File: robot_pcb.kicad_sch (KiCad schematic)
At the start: 47 parts, among them J1 Raspberry_Pi_2_3, J10 Servo_TrayRelease, J11 BATT BYPASS, J12 12V BYPASS, J13 MAX14870, J14 MAX14870, J15 MAX14870, J16 MAX14870, J17 Conn_01x04, J18 USB_C_Receptacle_PowerOnly_6P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

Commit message: parts
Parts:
- C10, C11, C12, C13, C14, C15, C16, C6, C69, C7, C70, C8, C9: footprint (none) -> Capacitor_SMD:C_0402_1005Metric
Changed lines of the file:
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@@
 			)
 		)
-		(property "Footprint" ""
+		(property "Footprint" "Capacitor_SMD:C_0402_1005Metric"
 			(at 220.6752 102.87 0)
 			(effects
@@
 			)
 		)
-		(property "Footprint" ""
+		(property "Footprint" "Capacitor_SMD:C_0402_1005Metric"
 			(at 194.0052 48.26 0)
 			(effects
@@
 			)
 		)
-		(property "Footprint" ""
+		(property "Footprint" "Capacitor_SMD:C_0402_1005Metric"
 			(at 206.7052 48.26 0)
 			(effects
@@
 			)
 		)
-		(property "Footprint" ""
+		(property "Footprint" "Capacitor_SMD:C_0402_1005Metric"
 			(at 324.8152 48.26 0)
 			(effects
@@
 			)
 		)
-		(property "Footprint" ""
+		(property "Footprint" "Capacitor_SMD:C_0402_1005Metric"
 			(at 244.8052 48.26 0)
 			(effects
@@
 			)
 		)
-		(property "Footprint" ""
+		(property "Footprint" "Capacitor_SMD:C_0402_1005Metric"
 			(at 309.5752 48.26 0)
 			(effects
@@
 			)
 		)
-		(property "Footprint" ""
+		(property "Footprint" "Capacitor_SMD:C_0402_1005Metric"
 			(at 352.7552 48.26 0)
 			(effects
@@
 			)
 		)
-		(property "Footprint" ""
+		(property "Footprint" "Capacitor_SMD:C_0402_1005Metric"
 			(at 238.4552 102.87 0)
 			(effects
@@
 			)
 		)
-		(property "Footprint" ""
+		(property "Footprint" "Capacitor_SMD:C_0402_1005Metric"
 			(at 270.2052 48.26 0)
 			(effects
@@
 			)
 		)
-		(property "Footprint" ""
+		(property "Footprint" "Capacitor_SMD:C_0402_1005Metric"
 			(at 232.1052 48.26 0)
 			(effects
@@
 			)
 		)
-		(property "Footprint" ""
+		(property "Footprint" "Capacitor_SMD:C_0402_1005Metric"
 			(at 211.1248 62.23 0)
 			(effects
@@
 			)
 		)
-		(property "Footprint" ""
+		(property "Footprint" "Capacitor_SMD:C_0402_1005Metric"
 			(at 219.4052 48.26 0)
 			(effects
@@
 			)
 		)
-		(property "Footprint" ""
+		(property "Footprint" "Capacitor_SMD:C_0402_1005Metric"
 			(at 257.5052 48.26 0)
 			(effects

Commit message: part numebrs
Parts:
- C10, C11, C16, C6, C7, C8, C9: LCSC (none) -> C307331
- C12: footprint Capacitor_SMD:C_0402_1005Metric -> Capacitor_SMD:C_0603_1608Metric; LCSC (none) -> C96446
- C13: LCSC (none) -> C15195
- C14, C15: LCSC (none) -> C52923
- C69, C70: LCSC (none) -> C86285

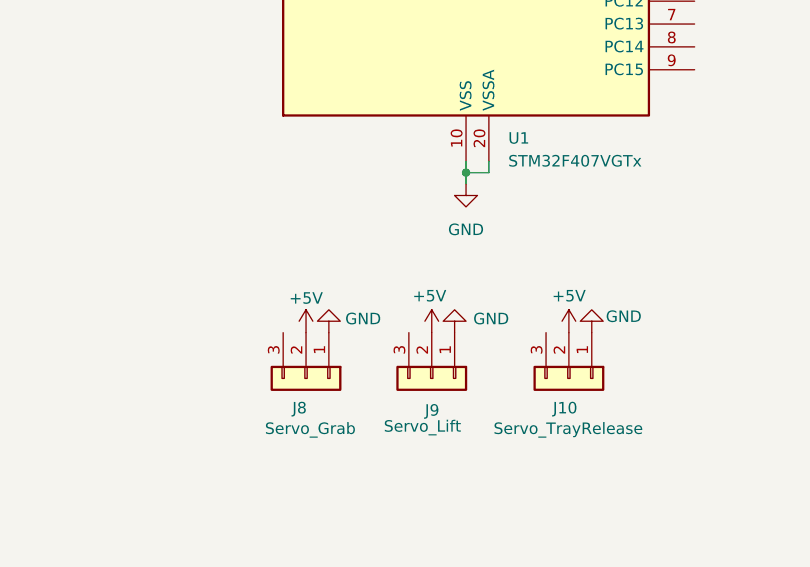
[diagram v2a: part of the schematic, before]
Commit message: added pwm to servos
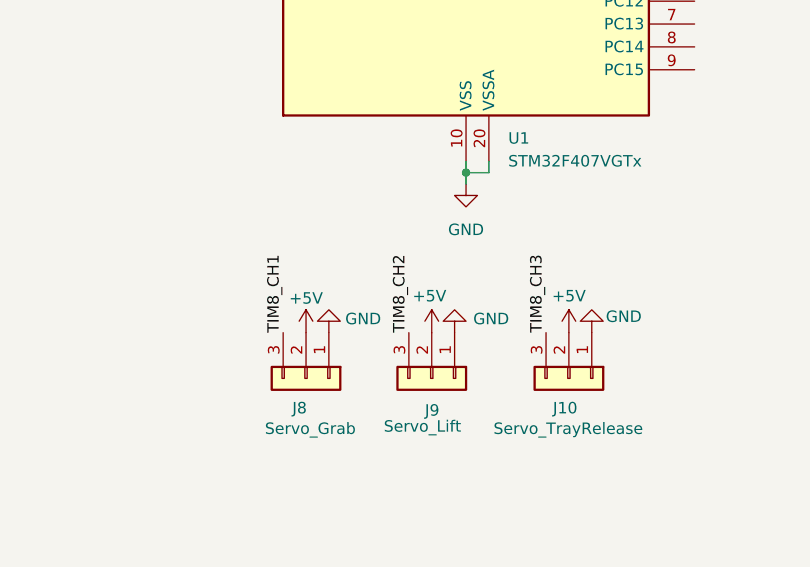
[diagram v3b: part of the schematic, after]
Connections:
- net TIM8_CH1: now also J8.3 (Pin_3)
- net TIM8_CH2: now also J9.3 (Pin_3)
- net TIM8_CH3: now also J10.3 (Pin_3)
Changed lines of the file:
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@@
+		)
+	)
+	(label "TIM8_CH2"
+		(at 284.48 214.63 90)
+		(effects
+			(font
+				(size 1.27 1.27)
+			)
+			(justify left bottom)
 		)
 	)
@@
 		)
 	)
+	(label "TIM8_CH1"
+		(at 270.51 214.63 90)
+		(effects
+			(font
+				(size 1.27 1.27)
+			)
+			(justify left bottom)
+		)
+	)
 	(label "BR_M2"
 		(at 124.46 261.62 0)
@@
 		(effects
 			(font
+				(size 1.27 1.27)
+			)
+			(justify left bottom)
+		)
+	)
+	(label "TIM8_CH3"
+		(at 299.72 214.63 90)
+		(effects
+			(font

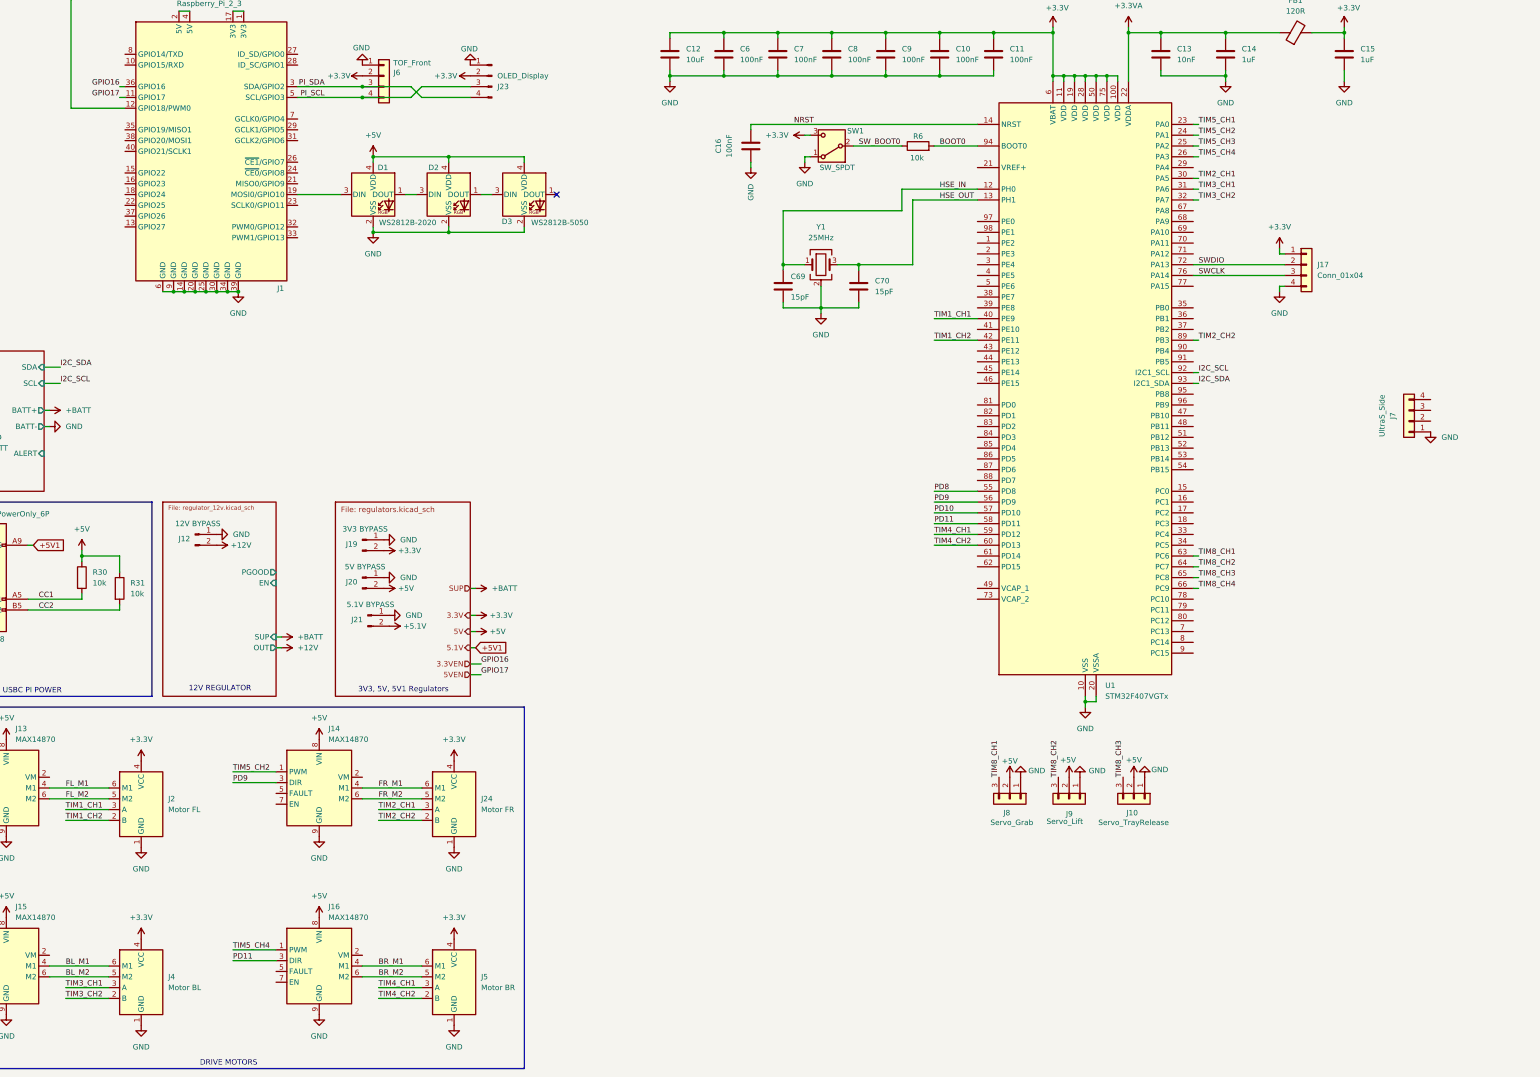
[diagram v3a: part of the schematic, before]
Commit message: Added BNO086
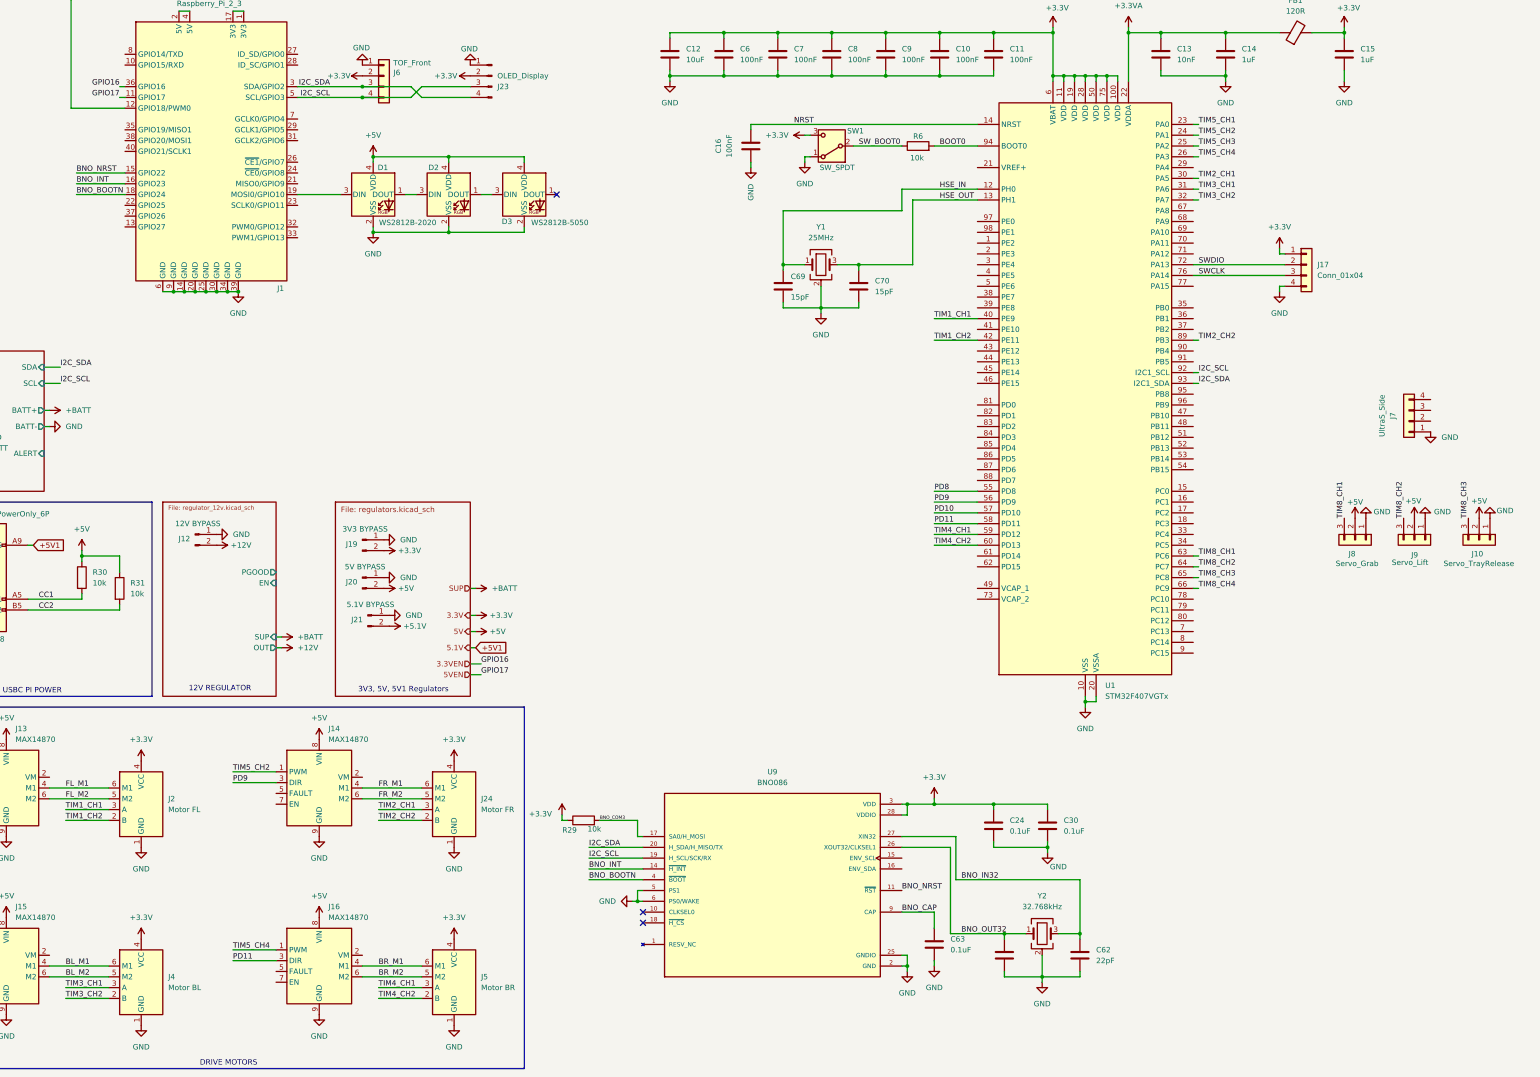
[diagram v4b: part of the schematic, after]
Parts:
- added C24, C30, C63: 0.1uF, Capacitor_SMD:C_0402_1005Metric, symbol Device:C
- added C61, C62: 22pF, Capacitor_SMD:C_0402_1005Metric, symbol Device:C
- added R29: 10k, Resistor_SMD:R_0402_1005Metric, symbol Device:R
- added U9: BNO086, International_Footprints:IC_BNO086, symbol International_Symbols:BNO086
- added Y2: 32.768kHz, symbol Device:Crystal_GND24
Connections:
- net PI_SCL is gone; now on net I2C_SCL: J1.5 (SCL/GPIO3), J6.4 (Pin_4)
- net PI_SDA is gone; now on net I2C_SDA: J1.3 (SDA/GPIO2), J6.3 (Pin_3)
- net +3.3V: now also C24.1, C30.1, R29.1, U9.28 (VDDIO), U9.3 (VDD)
- net GND: now also C24.2, C30.2, C61.2, C62.2, C63.2, U9.2 (GND), U9.25 (GNDIO), U9.5 (PS1), U9.6 (PS0/WAKE), Y2.2 (G), Y2.4 (G)
- net I2C_SCL: now also U9.19 (H_SCL/SCK/RX)
- net I2C_SDA: now also U9.20 (H_SDA/H_MISO/TX)
- net BNO_NRST: now reaches J1.15 (GPIO22)
- net BNO_NRST: now also U9.11 (~{RST})
- net BNO_INT: now reaches J1.16 (GPIO23)
- net BNO_INT: now also U9.14 (~{H_INT})
- net BNO_BOOTN: now reaches J1.18 (GPIO24)
- net BNO_BOOTN: now also U9.4 (~{BOOT})
- new net: U9.1 (RESV_NC), U9.12 (RESV_NC), U9.13 (RESV_NC), U9.21 (RESV_NC), U9.22 (RESV_NC), U9.23 (RESV_NC), U9.24 (RESV_NC), U9.7 (RESV_NC), U9.8 (RESV_NC)
- new net BNO_CAP: C63.1, U9.9 (CAP)
- new net BNO_COM3: R29.2, U9.17 (SA0/H_MOSI)
- new net BNO_IN32: C62.1, U9.27 (XIN32), Y2.3
- new net BNO_OUT32: C61.1, U9.26 (XOUT32/CLKSEL1), Y2.1
- no-connect marks 1 -> 3
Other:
- moved on the sheet: J10, J8, J9

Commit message: small changes
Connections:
- no-connect marks 3 -> 5
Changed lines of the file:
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@@
 	)
 	(no_connect
+		(at 247.65 236.22)
+	)
+	(no_connect
+		(at 247.65 233.68)
+	)
+	(no_connect
 		(at 186.69 248.92)
 	)
@@
 	(wire
 		(pts
+			(xy 172.72 228.6) (xy 186.69 228.6)
+		)
+		(stroke
+			(width 0)
+			(type default)
+		)
+	)
+	(wire
+		(pts
 			(xy 237.49 93.98) (xy 250.19 93.98)
 		)
@@
 	(wire
 		(pts
+			(xy 172.72 228.6) (xy 172.72 224.79)
+		)
+		(stroke
+			(width 0)
+			(type default)
+		)
+	)
+	(wire
+		(pts
 			(xy 50.8 266.7) (xy 60.96 266.7)
 		)
@@
 	(wire
 		(pts
-			(xy 255.27 147.32) (xy 265.43 147.32)
+			(xy 172.72 215.9) (xy 172.72 217.17)
 		)
 		(stroke
@@
 	(wire
 		(pts
-			(xy 308.61 40.64) (xy 308.61 39.37)
+			(xy 255.27 147.32) (xy 265.43 147.32)
 		)
 		(stroke
@@
 	(wire
 		(pts
-			(xy 167.64 223.52) (xy 167.64 224.79)
+			(xy 308.61 40.64) (xy 308.61 39.37)
 		)
 		(stroke
@@
 	(wire
 		(pts
-			(xy 185.42 228.6) (xy 186.69 228.6)
-		)
-		(stroke
-			(width 0)
-			(type default)
-		)
-	)
-	(wire
-		(pts
 			(xy 308.61 49.53) (xy 323.85 49.53)
 		)
@@
 	(wire
 		(pts
-			(xy 185.42 228.6) (xy 185.42 224.79)
-		)
-		(stroke
-			(width 0)
-			(type default)
-		)
-	)
-	(wire
-		(pts
 			(xy 247.65 81.28) (xy 247.65 76.2)
 		)
@@
 	(wire
 		(pts
-			(xy 176.53 224.79) (xy 185.42 224.79)
-		)
-		(stroke
-			(width 0)
-			(type default)
-		)
-	)
-	(wire
-		(pts
 			(xy 237.49 93.98) (xy 237.49 95.25)
 		)
@@
 	(wire
 		(pts
-			(xy 167.64 224.79) (xy 168.91 224.79)
-		)
-		(stroke
-			(width 0)
-			(type default)
-		)
-	)
-	(wire
-		(pts
 			(xy 247.65 220.98) (xy 248.92 220.98)
 		)
@@
 	)
 	(label "BNO_COM3"
-		(at 176.53 224.79 0)
+		(at 173.99 228.6 0)
 		(effects
 			(font
-				(size 0.762 0.762)
+				(size 1.27 1.27)
 			)
 			(justify left bottom)
@@
 	)
 	(symbol
+		(lib_id "Device:R")
+		(at 172.72 220.98 0)
+		(unit 1)
+		(exclude_from_sim no)
+		(in_bom yes)
+		(on_board yes)
+		(dnp no)
+		(fields_autoplaced yes)
+		(property "Reference" "R29"
+			(at 175.26 219.7099 0)
+			(effects
+				(font
+					(size 1.27 1.27)
+				)
+				(justify left)
+			)
+		)
+		(property "Value" "10k"
+			(at 175.26 222.2499 0)
+			(effects
+				(font
+					(size 1.27 1.27)
+				)
+				(justify left)
+			)
+		)
+		(property "Footprint" "Resistor_SMD:R_0402_1005Metric"
+			(at 170.942 220.98 90)
+			(effects
+				(font
+					(size 1.27 1.27)
+				)
+				(hide yes)
+			)
+		)
+		(property "Datasheet" "~"
+			(at 172.72 220.98 0)
+			(effects
+				(font
+					(size 1.27 1.27)
+				)
+				(hide yes)
+			)
+		)
+		(property "Description" "Resistor"
+			(at 172.72 220.98 0)
+			(effects
+				(font
+					(size 1.27 1.27)
+				)
+				(hide yes)
+			)
+		)
+		(pin "2"
+		)
+		(pin "1"
+		)
+		(instances
+			(project ""
+				(path "/2f56b371-1597-47e1-a48d-b7f69d342f77"
+					(reference "R29")
+					(unit 1)
+				)
+			)
+		)
+	)
+	(symbol
 		(lib_id "Switch:SW_SPDT")
 		(at 231.14 66.04 180)
@@
 	(symbol
 		(lib_id "power:+3.3V")
-		(at 167.64 223.52 0)
+		(at 172.72 215.9 0)
 		(unit 1)
 		(exclude_from_sim no)
@@
 		(dnp no)
 		(property "Reference" "#PWR091"
-			(at 167.64 227.33 0)
+			(at 172.72 219.71 0)
 			(effects
 				(font
@@
 		)
 		(property "Value" "+3.3V"
-			(at 162.56 223.266 0)
+			(at 167.64 215.646 0)
 			(effects
 				(font
@@
 		)
 		(property "Footprint" ""
-			(at 167.64 223.52 0)
+			(at 172.72 215.9 0)
 			(effects
 				(font
@@
 		)
 		(property "Datasheet" ""
-			(at 167.64 223.52 0)
+			(at 172.72 215.9 0)
 			(effects
 				(font
@@
 		)
 		(property "Description" "Power symbol creates a global label with name \"+3.3V\""
-			(at 167.64 223.52 0)
+			(at 172.72 215.9 0)
 			(effects
 				(font
@@
 					(unit 1)
 				)
-			)
-		)
-	)
-	(symbol
-		(lib_id "Device:R")
-		(at 172.72 224.79 90)
-		(unit 1)
-		(exclude_from_sim no)
-		(in_bom yes)
-		(on_board yes)
-		(dnp no)
-		(property "Reference" "R29"
-			(at 169.418 227.076 90)
-			(effects
-				(font
-					(size 1.27 1.27)
-				)
-			)
-		)
-		(property "Value" "10k"
-			(at 175.26 226.822 90)
-			(effects
-				(font
-					(size 1.27 1.27)
-				)
-			)
-		)
-		(property "Footprint" "Resistor_SMD:R_0402_1005Metric"
-			(at 172.72 226.568 90)
-			(effects
-				(font
-					(size 1.27 1.27)
-				)
-				(hide yes)
-			)
-		)
-		(property "Datasheet" "~"
-			(at 172.72 224.79 0)
-			(effects
-				(font
-					(size 1.27 1.27)
-				)
-				(hide yes)
-			)
-		)
-		(property "Description" "Resistor"
-			(at 172.72 224.79 0)
-			(effects
-				(font
-					(size 1.27 1.27)
-				)
-				(hide yes)
-			)
-		)
-		(pin "1"
-		)
-		(pin "2"
-		)
-		(instances
-			(project "robot_pcb"
-				(path "/2f56b371-1597-47e1-a48d-b7f69d342f77"
-					(reference "R29")
-					(unit 1)
-				)

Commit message: added some more footprints
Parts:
- FB1: footprint (none) -> Inductor_SMD:L_0603_1608Metric
- J17: footprint (none) -> Connector_PinHeader_2.54mm:PinHeader_1x04_P2.54mm_Vertical
- J18: footprint (none) -> Connector_USB:USB_C_Receptacle_GCT_USB4135-GF-A_6P_TopMnt_Horizontal
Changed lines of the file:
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@@
 			)
 		)
-		(property "Footprint" ""
+		(property "Footprint" "Inductor_SMD:L_0603_1608Metric"
 			(at 340.36 41.148 90)
 			(effects
@@
 			)
 		)
-		(property "Footprint" ""
+		(property "Footprint" "Connector_USB:USB_C_Receptacle_GCT_USB4135-GF-A_6P_TopMnt_Horizontal"
 			(at 30.48 165.1 0)
 			(effects
@@
 				)
 				(justify left)
-				(hide yes)
 			)
 		)
@@
 				)
 				(justify left)
-				(hide yes)
 			)
 		)
@@
 			)
 		)
-		(property "Footprint" ""
+		(property "Footprint" "Connector_PinHeader_2.54mm:PinHeader_1x04_P2.54mm_Vertical"
 			(at 342.9 93.98 0)
 			(effects
